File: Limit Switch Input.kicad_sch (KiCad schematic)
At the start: 3 parts

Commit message: Getting ready for fab
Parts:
- C?: DigiKey (none) -> 490-10700-1-ND
- R? (x2): DigiKey (none) -> 311-1.00KLRCT-ND
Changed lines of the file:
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@@
     (rev "0")
     (company "Cornell High Energy Synchrotron Source")
+    (comment 1 "Limit Switch Input Filtering")
     (comment 3 "S. Bywater")
     (comment 4 "S. Bywater")
@@
     )
     (property "Comments" "" (at 133.35 82.55 0)
+      (effects (font (size 1.27 1.27)) hide)
+    )
+    (property "DigiKey" "311-1.00KLRCT-ND" (at 133.35 82.55 0)
+      (effects (font (size 1.27 1.27)) hide)
+    )
+    (property "LCSC" "" (at 133.35 82.55 0)
       (effects (font (size 1.27 1.27)) hide)
     )
@@
       (effects (font (size 1.27 1.27)) hide)
     )
+    (property "DigiKey" "311-1.00KLRCT-ND" (at 127 76.2 0)
+      (effects (font (size 1.27 1.27)) hide)
+    )
+    (property "LCSC" "" (at 127 76.2 0)
+      (effects (font (size 1.27 1.27)) hide)
+    )
     (pin "1")
     (pin "2")
@@
       (effects (font (size 1.27 1.27)) hide)
     )
+    (property "DigiKey" "490-10700-1-ND" (at 139.7 82.55 0)
+      (effects (font (size 1.27 1.27)) hide)
+    )
+    (property "LCSC" "" (at 139.7 82.55 0)
+      (effects (font (size 1.27 1.27)) hide)
+    )

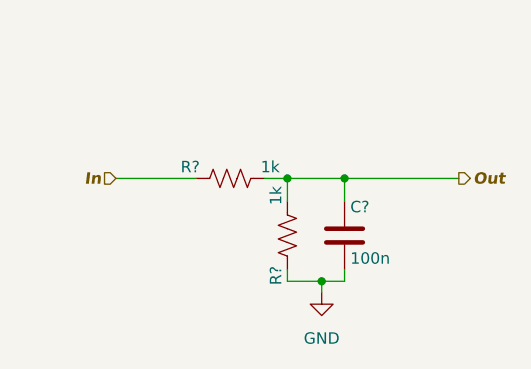
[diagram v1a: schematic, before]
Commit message: Limit switch inputs and silkscreen
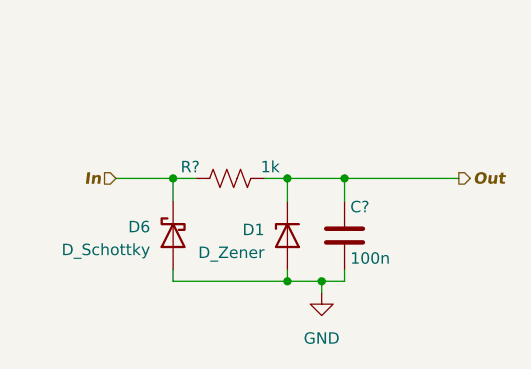
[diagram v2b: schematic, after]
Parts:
- removed R?: 1k, Resistor_SMD:R_0402_1005Metric, symbol Device:R_US
- added D1: D_Zener, Diode_SMD:D_SOD-523, symbol Device:D_Zener
- added D6: D_Schottky, Diode_SMD:D_SOD-523, symbol Device:D_Schottky
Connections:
- net GND: now also D1.2 (A), D6.2 (A)
- net In: now also D6.1 (K)
- net Out: now also D1.1 (K)
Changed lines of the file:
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@@
     (comment 4 "S. Bywater")
   )
+  (junction (at 120.65 76.2) (diameter 0) (color 0 0 0 0)
+  )
   (junction (at 133.35 76.2) (diameter 0) (color 0 0 0 0)
   )
@@
   (junction (at 137.16 87.63) (diameter 0) (color 0 0 0 0)
   )
+  (junction (at 133.35 87.63) (diameter 0) (color 0 0 0 0)
+  )
   (wire (pts (xy 133.35 76.2) (xy 139.7 76.2))
     (stroke (width 0) (type default))
@@
     (stroke (width 0) (type default))
   )
+  (wire (pts (xy 120.65 78.74) (xy 120.65 76.2))
+    (stroke (width 0) (type default))
+  )
+  (wire (pts (xy 120.65 86.36) (xy 120.65 87.63))
+    (stroke (width 0) (type default))
+  )
   (wire (pts (xy 130.81 76.2) (xy 133.35 76.2))
     (stroke (width 0) (type default))
   )
-  (wire (pts (xy 114.3 76.2) (xy 123.19 76.2))
+  (wire (pts (xy 114.3 76.2) (xy 120.65 76.2))
     (stroke (width 0) (type default))
   )
@@
     (stroke (width 0) (type default))
   )
+  (wire (pts (xy 120.65 87.63) (xy 133.35 87.63))
+    (stroke (width 0) (type default))
+  )
   (wire (pts (xy 137.16 88.9) (xy 137.16 87.63))
+    (stroke (width 0) (type default))
+  )
+  (wire (pts (xy 120.65 76.2) (xy 123.19 76.2))
     (stroke (width 0) (type default))
   )
@@
     (effects (font (size 1.27 1.27) bold italic) (justify right))
   )
-  (symbol (lib_id "Device:R_US") (at 133.35 82.55 180) (unit 1)
-    (in_bom yes) (on_board yes) (dnp no)
-    (property "Reference" "R?" (at 132.08 86.995 90)
-      (effects (font (size 1.27 1.27)))
-    )
-    (property "Value" "1k" (at 132.08 78.105 90)
-      (effects (font (size 1.27 1.27)))
-    )
-    (property "Footprint" "Resistor_SMD:R_0402_1005Metric" (at 132.334 82.296 90)
+  (symbol (lib_id "Device:D_Zener") (at 133.35 82.55 90) (mirror x) (unit 1)
+    (in_bom yes) (on_board yes) (dnp no)
+    (property "Reference" "D1" (at 130.81 81.915 90)
+      (effects (font (size 1.27 1.27)) (justify left))
+    )
+    (property "Value" "D_Zener" (at 130.81 84.455 90)
+      (effects (font (size 1.27 1.27)) (justify left))
+    )
+    (property "Footprint" "Diode_SMD:D_SOD-523" (at 133.35 82.55 0)
       (effects (font (size 1.27 1.27)) hide)
     )
@@
       (effects (font (size 1.27 1.27)) hide)
     )
-    (property "Comments" "" (at 133.35 82.55 0)
-      (effects (font (size 1.27 1.27)) hide)
-    )
-    (property "DigiKey" "311-1.00KLRCT-ND" (at 133.35 82.55 0)
-      (effects (font (size 1.27 1.27)) hide)
-    )
-    (property "LCSC" "" (at 133.35 82.55 0)
-      (effects (font (size 1.27 1.27)) hide)
-    )
-    (pin "1")
-    (pin "2")
-    (instances
-      (project "ECE4760 Motor Driver"
-        (path "/6b38a626-de8c-4b2d-bc76-3a02bc823a86"
-          (reference "R?") (unit 1)
-        )
-        (path "/6b38a626-de8c-4b2d-bc76-3a02bc823a86/9895140f-573d-481d-a8a6-67e4fef141c0"
-          (reference "R36") (unit 1)
-        )
-        (path "/6b38a626-de8c-4b2d-bc76-3a02bc823a86/299487ec-ee2d-43f4-ae82-35783d2e6b45"
-          (reference "R38") (unit 1)
-        )
-        (path "/6b38a626-de8c-4b2d-bc76-3a02bc823a86/5fa307ae-0220-4647-a069-86a82689cac4"
-          (reference "R40") (unit 1)
-        )
-        (path "/6b38a626-de8c-4b2d-bc76-3a02bc823a86/3c576bdf-2a9b-47b5-bf2f-8d65e4282c90"
-          (reference "R42") (unit 1)
+    (property "DigiKey" "BZT52C3V3T-7DICT-ND" (at 133.35 82.55 90)
+      (effects (font (size 1.27 1.27)) hide)
+    )
+    (property "LCSC" "C151563" (at 133.35 82.55 90)
+      (effects (font (size 1.27 1.27)) hide)
+    )
+    (pin "1")
+    (pin "2")
+    (instances
+      (project "ECE4760 Motor Driver"
+        (path "/6b38a626-de8c-4b2d-bc76-3a02bc823a86/9895140f-573d-481d-a8a6-67e4fef141c0"
+          (reference "D1") (unit 1)
+        )
+        (path "/6b38a626-de8c-4b2d-bc76-3a02bc823a86/299487ec-ee2d-43f4-ae82-35783d2e6b45"
+          (reference "D3") (unit 1)
+        )
+        (path "/6b38a626-de8c-4b2d-bc76-3a02bc823a86/5fa307ae-0220-4647-a069-86a82689cac4"
+          (reference "D4") (unit 1)
+        )
+        (path "/6b38a626-de8c-4b2d-bc76-3a02bc823a86/3c576bdf-2a9b-47b5-bf2f-8d65e4282c90"
+          (reference "D5") (unit 1)
         )
       )
@@
         )
       )
+    )
+  )
+  (symbol (lib_id "Device:D_Schottky") (at 120.65 82.55 90) (mirror x) (unit 1)
+    (in_bom yes) (on_board yes) (dnp no)
+    (property "Reference" "D6" (at 118.11 81.5975 90)
+      (effects (font (size 1.27 1.27)) (justify left))
+    )
+    (property "Value" "D_Schottky" (at 118.11 84.1375 90)
+      (effects (font (size 1.27 1.27)) (justify left))
+    )
+    (property "Footprint" "Diode_SMD:D_SOD-523" (at 120.65 82.55 0)
+      (effects (font (size 1.27 1.27)) hide)
+    )
+    (property "Datasheet" "~" (at 120.65 82.55 0)
+      (effects (font (size 1.27 1.27)) hide)
+    )
+    (pin "1")
+    (pin "2")
+    (instances
+      (project "ECE4760 Motor Driver"
+        (path "/6b38a626-de8c-4b2d-bc76-3a02bc823a86/9895140f-573d-481d-a8a6-67e4fef141c0"
+          (reference "D6") (unit 1)
+        )
+        (path "/6b38a626-de8c-4b2d-bc76-3a02bc823a86/299487ec-ee2d-43f4-ae82-35783d2e6b45"
+          (reference "D7") (unit 1)
+        )
+        (path "/6b38a626-de8c-4b2d-bc76-3a02bc823a86/5fa307ae-0220-4647-a069-86a82689cac4"
+          (reference "D8") (unit 1)
+        )
+        (path "/6b38a626-de8c-4b2d-bc76-3a02bc823a86/3c576bdf-2a9b-47b5-bf2f-8d65e4282c90"
+          (reference "D9") (unit 1)
+        )
+      )

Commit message: Ready for design review
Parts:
- removed D1: D_Zener, Diode_SMD:D_SOD-523, symbol Device:D_Zener
- removed D6: D_Schottky, Diode_SMD:D_SOD-523, symbol Device:D_Schottky
- added D?: BAT54XY, Package_TO_SOT_SMD:SOT-363_SC-70-6, symbol Diode:BAT54SW
- added R22: 4k7, Resistor_SMD:R_0402_1005Metric, symbol Device:R_US
- C?: DigiKey 490-10700-1-ND -> 490-3261-1-ND; LCSC (none) -> C71629
- R?: value 1k -> 100; DigiKey 311-1.00KLRCT-ND -> 311-100JRCT-ND; LCSC (none) -> C106233
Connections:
- net GND: now also D?.1 (A)
- net Out: now also D?.6 (COM), R22.2
- new net +5V: D?.2 (K), R22.1
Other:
- moved on the sheet: C?, R?

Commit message: Update
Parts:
- removed D?: BAT54XY, Package_TO_SOT_SMD:SOT-363_SC-70-6, symbol Diode:BAT54SW
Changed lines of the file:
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@@
     (comment 4 "S. Bywater")
   )
-  (junction (at 127 76.2) (diameter 0) (color 0 0 0 0)
-  )
-  (junction (at 130.175 88.265) (diameter 0) (color 0 0 0 0)
-  )
   (junction (at 133.35 76.2) (diameter 0) (color 0 0 0 0)
   )
-  (junction (at 130.175 64.135) (diameter 0) (color 0 0 0 0)
-  )
-  (wire (pts (xy 127 64.135) (xy 130.175 64.135))
-    (stroke (width 0) (type default))
-  )
   (wire (pts (xy 133.35 76.2) (xy 139.7 76.2))
     (stroke (width 0) (type default))
@@
     (stroke (width 0) (type default))
   )
-  (wire (pts (xy 121.285 76.2) (xy 127 76.2))
-    (stroke (width 0) (type default))
-  )
-  (wire (pts (xy 130.175 63.5) (xy 130.175 64.135))
+  (wire (pts (xy 121.285 76.2) (xy 133.35 76.2))
+    (stroke (width 0) (type default))
+  )
+  (wire (pts (xy 133.35 63.5) (xy 133.35 66.04))
     (stroke (width 0) (type default))
   )
@@
     (stroke (width 0) (type default))
   )
-  (wire (pts (xy 130.175 64.135) (xy 133.35 64.135))
-    (stroke (width 0) (type default))
-  )
-  (wire (pts (xy 130.175 88.265) (xy 133.35 88.265))
-    (stroke (width 0) (type default))
-  )
-  (wire (pts (xy 130.175 88.265) (xy 130.175 88.9))
-    (stroke (width 0) (type default))
-  )
   (wire (pts (xy 107.95 76.2) (xy 113.665 76.2))
     (stroke (width 0) (type default))
   )
-  (wire (pts (xy 130.175 88.265) (xy 127 88.265))
-    (stroke (width 0) (type default))
-  )
-  (wire (pts (xy 127 88.265) (xy 127 83.82))
-    (stroke (width 0) (type default))
-  )
-  (wire (pts (xy 133.35 88.265) (xy 133.35 86.36))
-    (stroke (width 0) (type default))
-  )
-  (wire (pts (xy 127 76.2) (xy 133.35 76.2))
-    (stroke (width 0) (type default))
-  )
-  (wire (pts (xy 133.35 64.135) (xy 133.35 66.04))
-    (stroke (width 0) (type default))
-  )
-  (wire (pts (xy 127 68.58) (xy 127 64.135))
+  (wire (pts (xy 133.35 86.36) (xy 133.35 88.9))
     (stroke (width 0) (type default))
   )
@@
           (reference "R24") (unit 1)
         )
-        (path "/6b38a626-de8c-4b2d-bc76-3a02bc823a86/3c576bdf-2a9b-47b5-bf2f-8d65e4282c90"
-          (reference "R26") (unit 1)
-        )
-      )
-    )
-  )
-  (symbol (lib_id "power:GND") (at 130.175 88.9 0) (unit 1)
+      )
+    )
+  )
+  (symbol (lib_id "power:GND") (at 133.35 88.9 0) (unit 1)
     (in_bom yes) (on_board yes) (dnp no) (fields_autoplaced)
-    (property "Reference" "#PWR010" (at 130.175 95.25 0)
-      (effects (font (size 1.27 1.27)) hide)
-    )
-    (property "Value" "GND" (at 130.175 93.98 0)
-      (effects (font (size 1.27 1.27)) hide)
-    )
-    (property "Footprint" "" (at 130.175 88.9 0)
-      (effects (font (size 1.27 1.27)) hide)
-    )
-    (property "Datasheet" "" (at 130.175 88.9 0)
+    (property "Reference" "#PWR010" (at 133.35 95.25 0)
+      (effects (font (size 1.27 1.27)) hide)
+    )
+    (property "Value" "GND" (at 133.35 93.98 0)
+      (effects (font (size 1.27 1.27)) hide)
+    )
+    (property "Footprint" "" (at 133.35 88.9 0)
+      (effects (font (size 1.27 1.27)) hide)
+    )
+    (property "Datasheet" "" (at 133.35 88.9 0)
       (effects (font (size 1.27 1.27)) hide)
     )
@@
         (path "/6b38a626-de8c-4b2d-bc76-3a02bc823a86/5fa307ae-0220-4647-a069-86a82689cac4"
           (reference "#PWR014") (unit 1)
-        )
-        (path "/6b38a626-de8c-4b2d-bc76-3a02bc823a86/3c576bdf-2a9b-47b5-bf2f-8d65e4282c90"
-          (reference "#PWR016") (unit 1)
-        )
-      )
-    )
-  )
-  (symbol (lib_id "Diode:BAT54SW") (at 127 76.2 90) (unit 1)
-    (in_bom yes) (on_board yes) (dnp no)
-    (property "Reference" "D?" (at 125.095 68.58 90)
-      (effects (font (size 1.27 1.27)) (justify left))
-    )
-    (property "Value" "BAT54XY" (at 125.095 70.485 90)
-      (effects (font (size 1.27 1.27)) (justify left))
-    )
-    (property "Footprint" "Package_TO_SOT_SMD:SOT-363_SC-70-6" (at 130.81 76.2 0)
-      (effects (font (size 1.27 1.27)) (justify left) hide)
-    )
-    (property "Datasheet" "https://assets.nexperia.com/documents/data-sheet/BAT54W_SER.pdf" (at 130.81 76.2 0)
-      (effects (font (size 1.27 1.27)) hide)
-    )
-    (property "LCSC" "C282367" (at 127 76.2 0)
-      (effects (font (size 1.27 1.27)) hide)
-    )
-    (property "DigiKey" "1727-3571-1-ND" (at 127 76.2 0)
-      (effects (font (size 1.27 1.27)) hide)
-    )
-    (pin "1")
-    (pin "2")
-    (pin "6")
-    (pin "3")
-    (pin "4")
-    (pin "5")
-    (instances
-      (project "ECE4760 Motor Driver"
-        (path "/6b38a626-de8c-4b2d-bc76-3a02bc823a86"
-          (reference "D?") (unit 1)
-        )
-        (path "/6b38a626-de8c-4b2d-bc76-3a02bc823a86/9895140f-573d-481d-a8a6-67e4fef141c0"
-          (reference "D3") (unit 1)
-        )
-        (path "/6b38a626-de8c-4b2d-bc76-3a02bc823a86/299487ec-ee2d-43f4-ae82-35783d2e6b45"
-          (reference "D3") (unit 2)
-        )
-        (path "/6b38a626-de8c-4b2d-bc76-3a02bc823a86/5fa307ae-0220-4647-a069-86a82689cac4"
-          (reference "D4") (unit 1)
-        )
-        (path "/6b38a626-de8c-4b2d-bc76-3a02bc823a86/3c576bdf-2a9b-47b5-bf2f-8d65e4282c90"
-          (reference "D4") (unit 2)
         )
       )
@@
           (reference "R25") (unit 1)
         )
-        (path "/6b38a626-de8c-4b2d-bc76-3a02bc823a86/3c576bdf-2a9b-47b5-bf2f-8d65e4282c90"
-          (reference "R27") (unit 1)
-        )
-      )
-    )
-  )
-  (symbol (lib_id "power:+5V") (at 130.175 63.5 0) (unit 1)
+      )
+    )
+  )
+  (symbol (lib_id "power:+5V") (at 133.35 63.5 0) (unit 1)
     (in_bom yes) (on_board yes) (dnp no) (fields_autoplaced)
-    (property "Reference" "#PWR011" (at 130.175 67.31 0)
-      (effects (font (size 1.27 1.27)) hide)
-    )
-    (property "Value" "+5V" (at 130.175 59.69 0)
+    (property "Reference" "#PWR011" (at 133.35 67.31 0)
+      (effects (font (size 1.27 1.27)) hide)
+    )
+    (property "Value" "+5V" (at 133.35 59.69 0)
       (effects (font (size 1.27 1.27)))
     )
-    (property "Footprint" "" (at 130.175 63.5 0)
-      (effects (font (size 1.27 1.27)) hide)
-    )
-    (property "Datasheet" "" (at 130.175 63.5 0)
+    (property "Footprint" "" (at 133.35 63.5 0)
+      (effects (font (size 1.27 1.27)) hide)
+    )
+    (property "Datasheet" "" (at 133.35 63.5 0)
       (effects (font (size 1.27 1.27)) hide)
     )
@@
         (path "/6b38a626-de8c-4b2d-bc76-3a02bc823a86/5fa307ae-0220-4647-a069-86a82689cac4"
           (reference "#PWR013") (unit 1)
-        )
-        (path "/6b38a626-de8c-4b2d-bc76-3a02bc823a86/3c576bdf-2a9b-47b5-bf2f-8d65e4282c90"
-          (reference "#PWR015") (unit 1)
         )
       )
@@
           (reference "C67") (unit 1)
         )
-        (path "/6b38a626-de8c-4b2d-bc76-3a02bc823a86/3c576bdf-2a9b-47b5-bf2f-8d65e4282c90"
-          (reference "C68") (unit 1)
-        )
-      )
+      )

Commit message: Boards ordered!
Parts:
- renumbered R22 to R30
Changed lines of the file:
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@@
   (symbol (lib_id "Device:R_US") (at 133.35 69.85 0) (unit 1)
     (in_bom yes) (on_board yes) (dnp no) (fields_autoplaced)
-    (property "Reference" "R22" (at 135.89 69.215 0)
+    (property "Reference" "R30" (at 135.89 69.215 0)
       (effects (font (size 1.27 1.27)) (justify left))
     )
@@
       (project "ECE4760 Motor Driver"
         (path "/6b38a626-de8c-4b2d-bc76-3a02bc823a86/299487ec-ee2d-43f4-ae82-35783d2e6b45"
-          (reference "R22") (unit 1)
+          (reference "R30") (unit 1)
         )
         (path "/6b38a626-de8c-4b2d-bc76-3a02bc823a86/9895140f-573d-481d-a8a6-67e4fef141c0"
-          (reference "R20") (unit 1)
+          (reference "R28") (unit 1)
         )
         (path "/6b38a626-de8c-4b2d-bc76-3a02bc823a86/5fa307ae-0220-4647-a069-86a82689cac4"
-          (reference "R24") (unit 1)
+          (reference "R32") (unit 1)
         )
       )
@@
   (symbol (lib_id "power:GND") (at 133.35 88.9 0) (unit 1)
     (in_bom yes) (on_board yes) (dnp no) (fields_autoplaced)
-    (property "Reference" "#PWR010" (at 133.35 95.25 0)
+    (property "Reference" "#PWR078" (at 133.35 95.25 0)
       (effects (font (size 1.27 1.27)) hide)
     )
@@
       (project "ECE4760 Motor Driver"
         (path "/6b38a626-de8c-4b2d-bc76-3a02bc823a86/9895140f-573d-481d-a8a6-67e4fef141c0"
-          (reference "#PWR010") (unit 1)
+          (reference "#PWR078") (unit 1)
         )
         (path "/6b38a626-de8c-4b2d-bc76-3a02bc823a86/299487ec-ee2d-43f4-ae82-35783d2e6b45"
-          (reference "#PWR012") (unit 1)
+          (reference "#PWR080") (unit 1)
         )
         (path "/6b38a626-de8c-4b2d-bc76-3a02bc823a86/5fa307ae-0220-4647-a069-86a82689cac4"
-          (reference "#PWR014") (unit 1)
+          (reference "#PWR082") (unit 1)
         )
       )
@@
         )
         (path "/6b38a626-de8c-4b2d-bc76-3a02bc823a86/9895140f-573d-481d-a8a6-67e4fef141c0"
-          (reference "R21") (unit 1)
+          (reference "R29") (unit 1)
         )
         (path "/6b38a626-de8c-4b2d-bc76-3a02bc823a86/299487ec-ee2d-43f4-ae82-35783d2e6b45"
-          (reference "R23") (unit 1)
+          (reference "R31") (unit 1)
         )
         (path "/6b38a626-de8c-4b2d-bc76-3a02bc823a86/5fa307ae-0220-4647-a069-86a82689cac4"
-          (reference "R25") (unit 1)
+          (reference "R33") (unit 1)
         )
       )
@@
   (symbol (lib_id "power:+5V") (at 133.35 63.5 0) (unit 1)
     (in_bom yes) (on_board yes) (dnp no) (fields_autoplaced)
-    (property "Reference" "#PWR011" (at 133.35 67.31 0)
+    (property "Reference" "#PWR079" (at 133.35 67.31 0)
       (effects (font (size 1.27 1.27)) hide)
     )
@@
       (project "ECE4760 Motor Driver"
         (path "/6b38a626-de8c-4b2d-bc76-3a02bc823a86/299487ec-ee2d-43f4-ae82-35783d2e6b45"
-          (reference "#PWR011") (unit 1)
+          (reference "#PWR079") (unit 1)
         )
         (path "/6b38a626-de8c-4b2d-bc76-3a02bc823a86/9895140f-573d-481d-a8a6-67e4fef141c0"
-          (reference "#PWR09") (unit 1)
+          (reference "#PWR077") (unit 1)
         )
         (path "/6b38a626-de8c-4b2d-bc76-3a02bc823a86/5fa307ae-0220-4647-a069-86a82689cac4"
-          (reference "#PWR013") (unit 1)
+          (reference "#PWR081") (unit 1)
         )
       )
@@
         )
         (path "/6b38a626-de8c-4b2d-bc76-3a02bc823a86/9895140f-573d-481d-a8a6-67e4fef141c0"
-          (reference "C65") (unit 1)
+          (reference "C46") (unit 1)
         )
         (path "/6b38a626-de8c-4b2d-bc76-3a02bc823a86/299487ec-ee2d-43f4-ae82-35783d2e6b45"
-          (reference "C66") (unit 1)
+          (reference "C47") (unit 1)
         )
         (path "/6b38a626-de8c-4b2d-bc76-3a02bc823a86/5fa307ae-0220-4647-a069-86a82689cac4"
-          (reference "C67") (unit 1)
+          (reference "C48") (unit 1)
         )
       )
